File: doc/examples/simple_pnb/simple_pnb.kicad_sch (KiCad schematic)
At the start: 5 parts

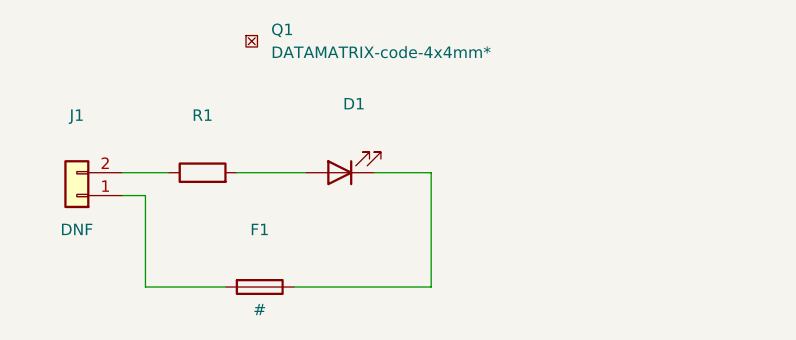
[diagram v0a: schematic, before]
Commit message: Update the example so custom tab symbols are used
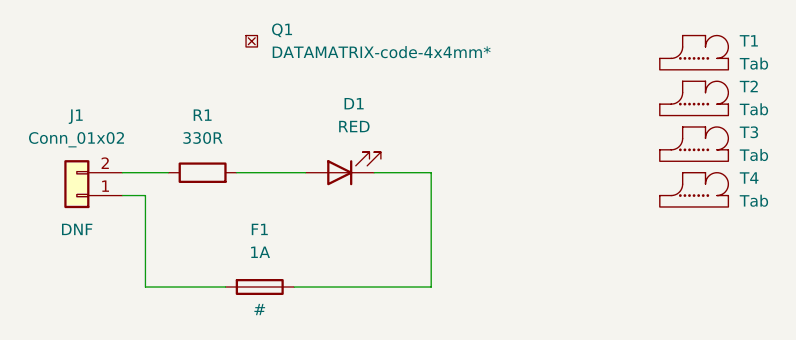
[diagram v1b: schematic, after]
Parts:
- added T1, T2, T3, T4: Tab, prusa_other:Tab_2mm, symbol kikit:Tab
- D1: value (none) -> RED; footprint (none) -> LED_SMD:LED_0603_1608Metric
- F1: value (none) -> 1A; footprint (none) -> Fuse:Fuse_Blade_ATO_directSolder
- J1: value (none) -> Conn_01x02; footprint (none) -> Connector_PinHeader_2.54mm:PinHeader_1x02_P2.54mm_Horizontal
- Q1: value (none) -> G_DATAMATRIX-code-4x4mm*; footprint (none) -> prusa_other:Datamatyrix-code-4x4mm
- R1: value (none) -> 330R; footprint (none) -> Resistor_SMD:R_0603_1608Metric
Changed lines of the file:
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@@
     (stroke (width 0) (type default) (color 0 0 0 0))
+  )
+  (symbol (lib_id "kikit:Tab") (at 189.23 76.2 0) (unit 1)
+    (in_bom no) (on_board yes) (fields_autoplaced)
+    (property "Reference" "T4" (id 0) (at 194.31 74.2949 0)
+      (effects (font (size 1.27 1.27)) (justify left))
+    )
+    (property "Value" "Tab" (id 1) (at 194.31 76.8349 0)
+      (effects (font (size 1.27 1.27)) (justify left))
+    )
+    (property "Footprint" "prusa_other:Tab_2mm" (id 2) (at 189.23 76.2 0)
+      (effects (font (size 1.27 1.27)) hide)
+    )
+    (property "Datasheet" "" (id 3) (at 189.23 76.2 0)
+      (effects (font (size 1.27 1.27)) hide)
+    )
+    (property "PnB" "dnf" (id 4) (at 189.23 76.2 0)
+      (effects (font (size 1.27 1.27)) hide)
+    )
+  )
+  (symbol (lib_id "kikit:Tab") (at 189.23 66.04 0) (unit 1)
+    (in_bom no) (on_board yes) (fields_autoplaced)
+    (property "Reference" "T2" (id 0) (at 194.31 64.1349 0)
+      (effects (font (size 1.27 1.27)) (justify left))
+    )
+    (property "Value" "Tab" (id 1) (at 194.31 66.6749 0)
+      (effects (font (size 1.27 1.27)) (justify left))
+    )
+    (property "Footprint" "prusa_other:Tab_2mm" (id 2) (at 189.23 66.04 0)
+      (effects (font (size 1.27 1.27)) hide)
+    )
+    (property "Datasheet" "" (id 3) (at 189.23 66.04 0)
+      (effects (font (size 1.27 1.27)) hide)
+    )
+    (property "PnB" "dnf" (id 4) (at 189.23 66.04 0)
+      (effects (font (size 1.27 1.27)) hide)
+    )
   )
   (symbol (lib_id "Connector_Generic:Conn_01x02") (at 120.65 76.2 180) (unit 1)
     (in_bom yes) (on_board yes)
     (property "Reference" "J1" (id 0) (at 120.65 67.31 0))
-    (property "Value" "" (id 1) (at 120.65 69.85 0))
-    (property "Footprint" "" (id 2) (at 120.65 76.2 0)
+    (property "Value" "Conn_01x02" (id 1) (at 120.65 69.85 0))
+    (property "Footprint" "Connector_PinHeader_2.54mm:PinHeader_1x02_P2.54mm_Horizontal" (id 2) (at 120.65 76.2 0)
       (effects (font (size 1.27 1.27)) hide)
     )
@@
     (pin "2")
   )
+  (symbol (lib_id "kikit:Tab") (at 189.23 60.96 0) (unit 1)
+    (in_bom no) (on_board yes) (fields_autoplaced)
+    (property "Reference" "T1" (id 0) (at 194.31 59.0549 0)
+      (effects (font (size 1.27 1.27)) (justify left))
+    )
+    (property "Value" "Tab" (id 1) (at 194.31 61.5949 0)
+      (effects (font (size 1.27 1.27)) (justify left))
+    )
+    (property "Footprint" "prusa_other:Tab_2mm" (id 2) (at 189.23 60.96 0)
+      (effects (font (size 1.27 1.27)) hide)
+    )
+    (property "Datasheet" "" (id 3) (at 189.23 60.96 0)
+      (effects (font (size 1.27 1.27)) hide)
+    )
+    (property "PnB" "dnf" (id 4) (at 189.23 60.96 0)
+      (effects (font (size 1.27 1.27)) hide)
+    )
+  )
   (symbol (lib_id "Device:R") (at 134.62 73.66 90) (unit 1)
     (in_bom yes) (on_board yes) (fields_autoplaced)
     (property "Reference" "R1" (id 0) (at 134.62 67.31 90))
-    (property "Value" "" (id 1) (at 134.62 69.85 90))
-    (property "Footprint" "" (id 2) (at 134.62 75.438 90)
+    (property "Value" "330R" (id 1) (at 134.62 69.85 90))
+    (property "Footprint" "Resistor_SMD:R_0603_1608Metric" (id 2) (at 134.62 75.438 90)
       (effects (font (size 1.27 1.27)) hide)
     )
@@
     (pin "2")
   )
+  (symbol (lib_id "kikit:Tab") (at 189.23 71.12 0) (unit 1)
+    (in_bom no) (on_board yes) (fields_autoplaced)
+    (property "Reference" "T3" (id 0) (at 194.31 69.2149 0)
+      (effects (font (size 1.27 1.27)) (justify left))
+    )
+    (property "Value" "Tab" (id 1) (at 194.31 71.7549 0)
+      (effects (font (size 1.27 1.27)) (justify left))
+    )
+    (property "Footprint" "prusa_other:Tab_2mm" (id 2) (at 189.23 71.12 0)
+      (effects (font (size 1.27 1.27)) hide)
+    )
+    (property "Datasheet" "" (id 3) (at 189.23 71.12 0)
+      (effects (font (size 1.27 1.27)) hide)
+    )
+    (property "PnB" "dnf" (id 4) (at 189.23 71.12 0)
+      (effects (font (size 1.27 1.27)) hide)
+    )
+  )
   (symbol (lib_id "prusa_other:G_DATAMATRIX-code-4x4mm*") (at 139.7 59.69 0) (unit 1)
     (in_bom yes) (on_board yes) (fields_autoplaced)
@@
       (effects (font (size 1.27 1.27)) (justify left))
     )
-    (property "Value" "" (id 1) (at 126.365 62.865 0)
+    (property "Value" "G_DATAMATRIX-code-4x4mm*" (id 1) (at 126.365 62.865 0)
       (effects (font (size 1.27 1.27)) (justify left) hide)
     )
-    (property "Footprint" "" (id 2) (at 139.7 60.96 0)
+    (property "Footprint" "prusa_other:Datamatyrix-code-4x4mm" (id 2) (at 139.7 60.96 0)
       (effects (font (size 1.27 1.27)) hide)
     )
@@
     (in_bom yes) (on_board yes)
     (property "Reference" "F1" (id 0) (at 140.97 80.01 90))
-    (property "Value" "" (id 1) (at 140.97 82.55 90))
-    (property "Footprint" "" (id 2) (at 140.97 84.582 90)
+    (property "Value" "1A" (id 1) (at 140.97 82.55 90))
+    (property "Footprint" "Fuse:Fuse_Blade_ATO_directSolder" (id 2) (at 140.97 84.582 90)
       (effects (font (size 1.27 1.27)) hide)
     )
@@
     (in_bom yes) (on_board yes) (fields_autoplaced)
     (property "Reference" "D1" (id 0) (at 151.4475 66.04 0))
-    (property "Value" "" (id 1) (at 151.4475 68.58 0))
-    (property "Footprint" "" (id 2) (at 149.86 73.66 0)
+    (property "Value" "RED" (id 1) (at 151.4475 68.58 0))
+    (property "Footprint" "LED_SMD:LED_0603_1608Metric" (id 2) (at 149.86 73.66 0)
       (effects (font (size 1.27 1.27)) hide)
     )
@@
       (reference "R1") (unit 1) (value "330R") (footprint "Resistor_SMD:R_0603_1608Metric")
     )
+    (path "/a8d7ca81-d6e2-41c7-8149-05f07adc3aea"
+      (reference "T1") (unit 1) (value "Tab") (footprint "prusa_other:Tab_2mm")
+    )
+    (path "/51525c3e-1a5c-4d35-a107-fea5f1555982"
+      (reference "T2") (unit 1) (value "Tab") (footprint "prusa_other:Tab_2mm")
+    )
+    (path "/b6372a50-b59e-4e59-b263-eeca7503a73b"
+      (reference "T3") (unit 1) (value "Tab") (footprint "prusa_other:Tab_2mm")
+    )
+    (path "/32d2e3cb-68e6-46fe-9e30-099d1aaaa859"
+      (reference "T4") (unit 1) (value "Tab") (footprint "prusa_other:Tab_2mm")
+    )
   )
